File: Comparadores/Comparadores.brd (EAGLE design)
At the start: 32 x 20.6 mm, 8 parts, among them IC1 LM358N

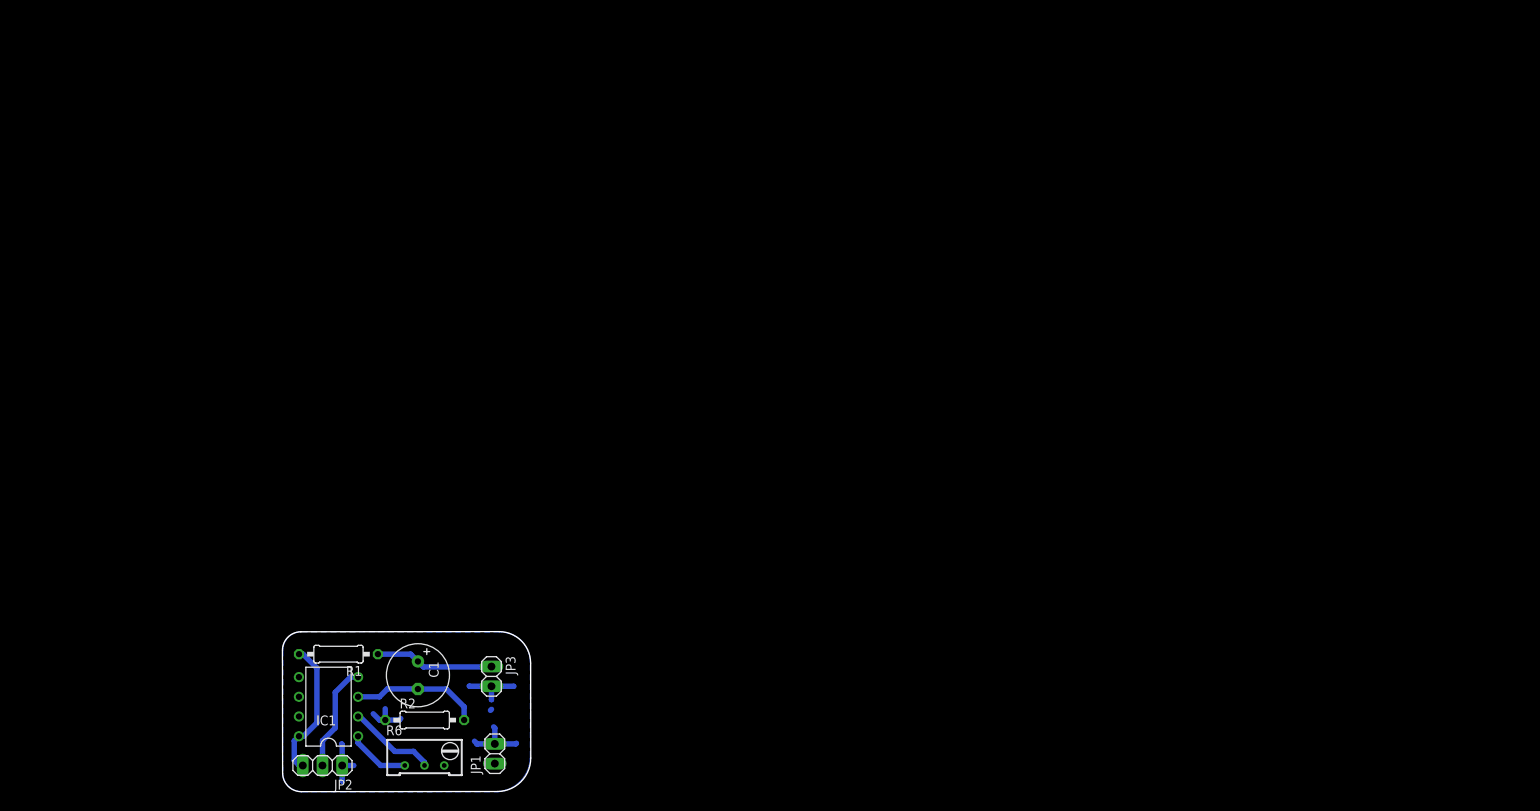
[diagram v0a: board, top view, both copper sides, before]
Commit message: Se agregan pistas para los filtros y se crean los comparadores
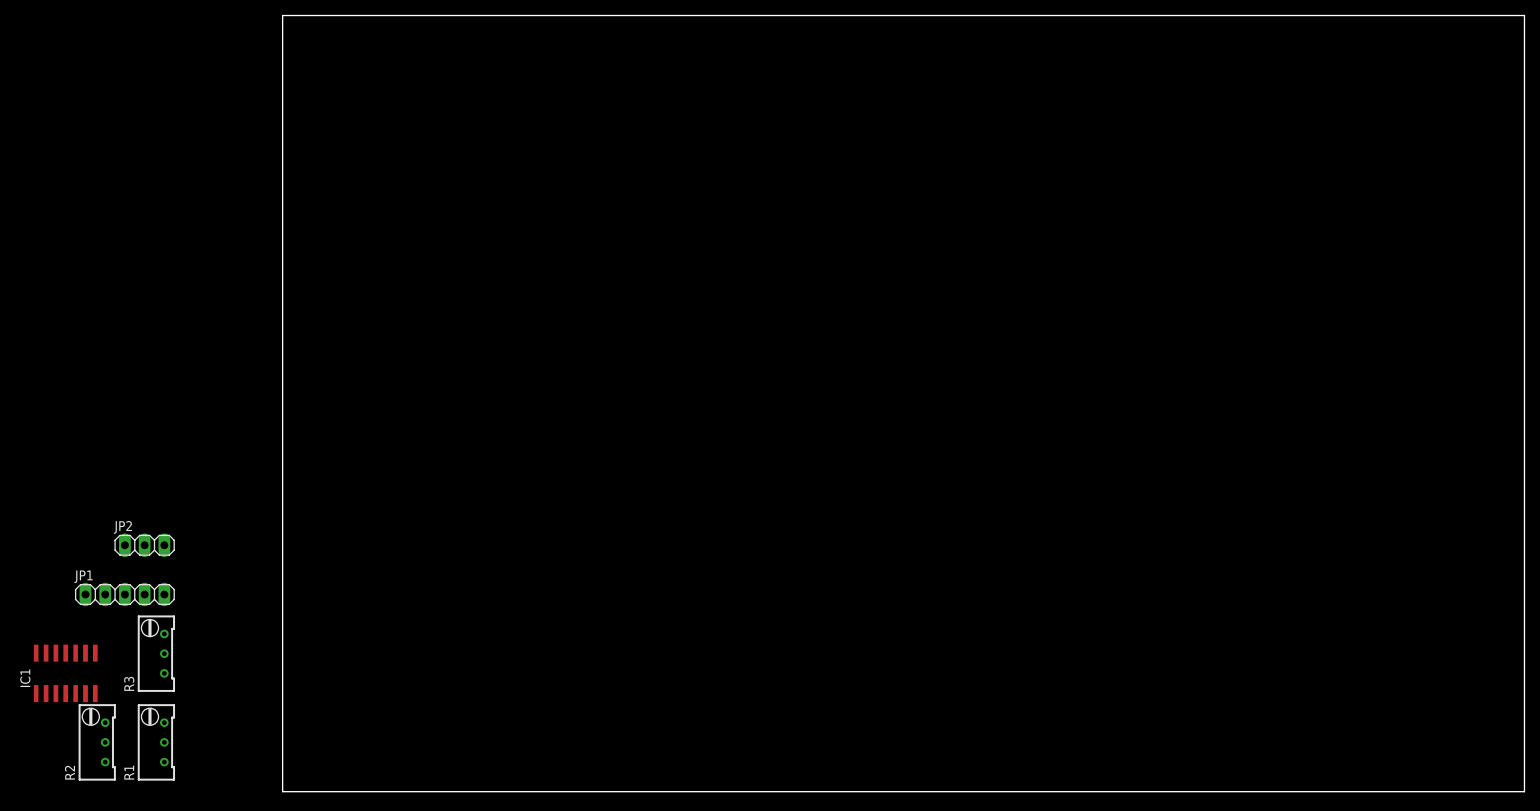
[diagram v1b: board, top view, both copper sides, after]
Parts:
- removed C1: 4.7u, rcl:E3,5-8
- removed JP3: (no value), pinhead:1X02
- removed R6: (no value), rcl:RTRIM64W
- added R3: (no value), rcl:RTRIM64W
- IC1: value LM358N -> LM324D; device linear:DIL08 -> linear:SO14
- JP1: device pinhead:1X02 -> pinhead:1X05
- R1: value 2.2k -> (none); device rcl:0207/10 -> rcl:RTRIM64W
- R2: value 10k -> (none); device rcl:0207/10 -> rcl:RTRIM64W
- moved JP1 51.9 mm to (-20.3, 25.4), turned to 0 degrees
- moved R2 42.5 mm to (-24.1, 6.35)
- moved JP2 36.5 mm to (-17.8, 31.8), turned to 0 degrees
- moved IC1 34.1 mm to (-27.9, 15.2), turned to 0 degrees
- moved R1 26.3 mm to (-16.5, 6.35), turned to 0 degrees
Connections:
- removed net 0: JP1.2, JP2.1, JP3.2, R2.1, R6.3
- removed net N$2: IC1.2, R6.2
- removed net V+: IC1.8, JP2.3, R1.2
- removed net V-: IC1.4, JP2.2
- removed net VAMP: IC1.1, JP1.1, R6.1
- removed net VO: C1.-, IC1.3, R2.2
- new net BAND: IC1.10, JP1.3
- new net CMPB: JP2.2
- new net CMPH: IC1.7, IC1.8, JP2.3
- new net CMPL: IC1.1, JP2.1
- new net GND: IC1.11, JP1.5, R1.1, R2.1, R3.1
- new net HIGH: IC1.5, JP1.4
- new net LOW: IC1.3, JP1.2
- new net N$16: IC1.9, R3.2
- new net N$3: IC1.6, R2.2
- new net VCC: IC1.4, JP1.1, R1.3, R2.3, R3.3
- net N$1: now also IC1.2, R1.2; no longer C1.+, JP3.1, R1.1
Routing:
- net 0: track 27.3 -> 0.00 mm
- net V+: track 17.9 -> 0.00 mm
- net VO: track 16.7 -> 0.00 mm
- net N$1: track 15.3 -> 0.00 mm
- net V-: track 13.9 -> 0.00 mm
- net N$2: track 11.4 -> 0.00 mm
- net VAMP: track 8.15 -> 0.00 mm
- removed copper zone on layer 16, net 0
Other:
- board size 32 x 20.6 mm -> 160 x 100 mm
